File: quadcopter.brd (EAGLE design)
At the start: 136.9 x 137 mm, 62 parts, among them J1 AVR_SPI_PRG_6NS, U1 ATMEGA128RFA1, Y1 16MHz

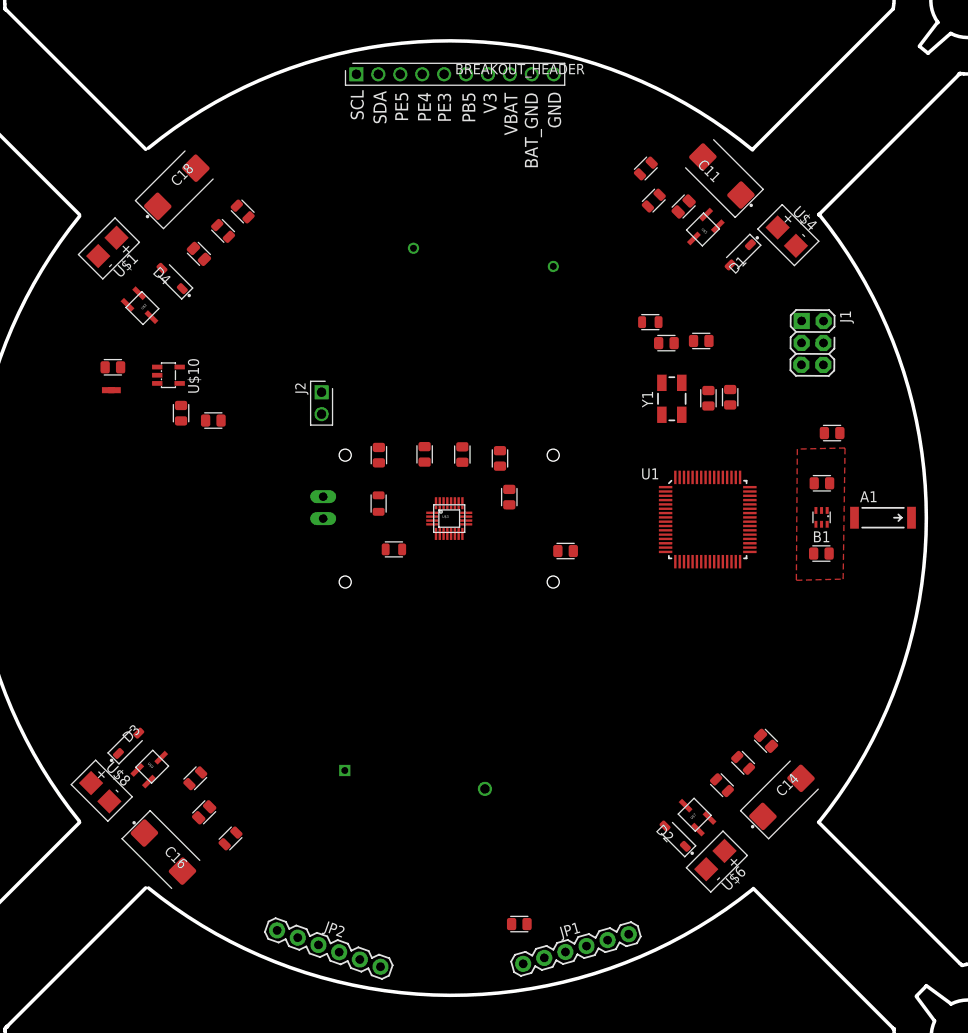
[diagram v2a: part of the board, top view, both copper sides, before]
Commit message: Trying to fix air wires
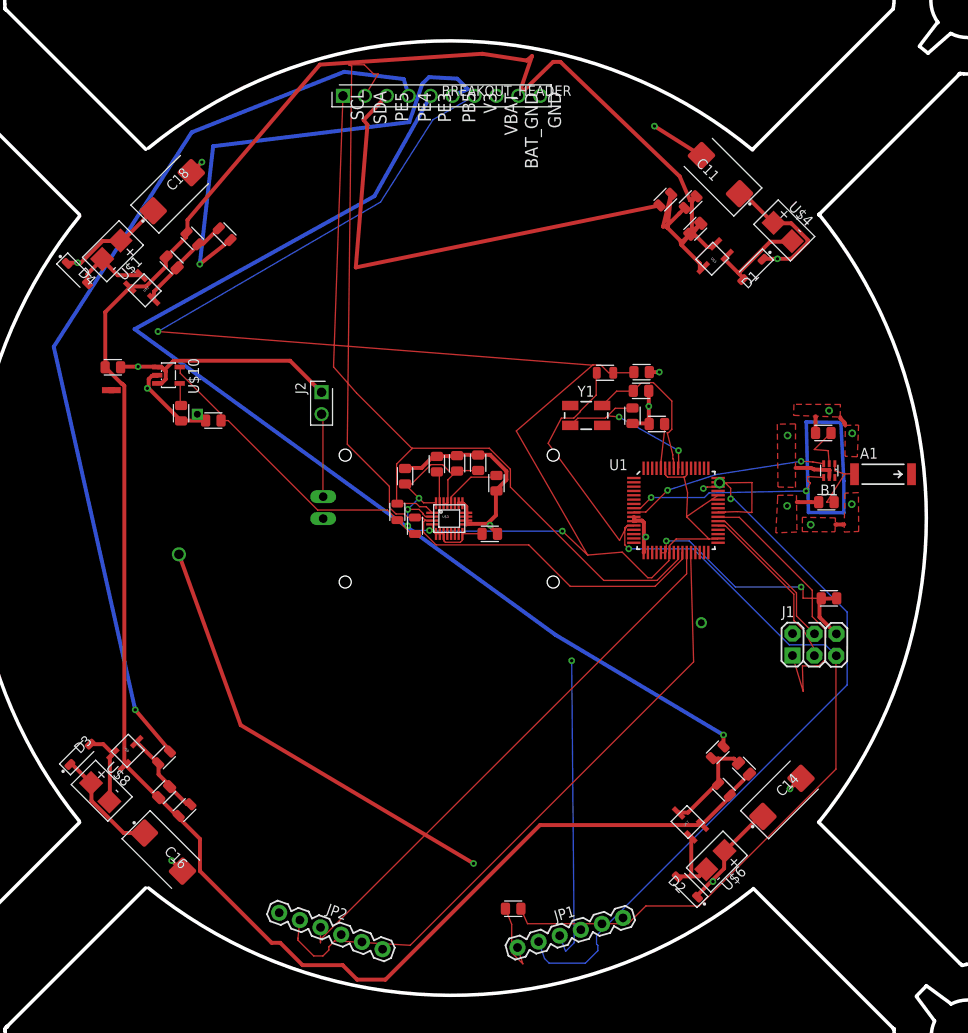
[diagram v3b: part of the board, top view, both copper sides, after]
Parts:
- moved J1 35.0 mm to (42.3, -14.6), turned to 359.7 degrees
- moved C28 19.2 mm to (44.0, -9.24)
- moved C12 14.0 mm to (43.3, 9.92)
- moved D4 11.0 mm to (-43.1, 28.4), turned to 315 degrees
- moved Y1 10.1 mm to (15.9, 11.9), turned to 0 degrees
- moved C27 9.06 mm to (22.2, 14.8)
- moved C29 9.04 mm to (24.1, 11.0), turned to 180 degrees
- moved C26 9.03 mm to (21.2, 11.9), turned to 270 degrees
- moved C5 9.00 mm to (4.70, -1.77)
- moved R1 7.88 mm to (18.1, 16.9)
- moved R6 6.49 mm to (28.0, 36.7)
- moved R10 6.26 mm to (-30.7, -33.8)
- moved D2 6.05 mm to (27.6, -42.7)
- moved D3 5.76 mm to (-42.8, -27.3)
- moved B1 5.49 mm to (44.0, 5.56)
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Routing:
- net V3: track 0.00 -> 260.9 mm, vias 0 -> 6
- net BAT_GND: track 0.00 -> 257.8 mm
- net PE3: track 0.00 -> 129.4 mm, vias 0 -> 1
- net VBAT: track 0.00 -> 123.6 mm, vias 0 -> 5
- net RESET: track 0.00 -> 118.2 mm, vias 0 -> 1
- net PE4: track 0.00 -> 107.0 mm, vias 0 -> 1
- net SDA: track 0.00 -> 102.1 mm
- net SCL: track 0.00 -> 96.4 mm
- net TX0: track 0.00 -> 82.3 mm, vias 0 -> 1
- net GND: track 0.00 -> 80.8 mm, vias 0 -> 15
- net TX1: track 0.00 -> 76.2 mm
- net RX1: track 0.00 -> 64.6 mm
- net RX0: track 0.00 -> 62.9 mm, vias 0 -> 2
- net PE5: track 0.00 -> 57.1 mm
- net PB5: track 0.00 -> 54.0 mm, vias 0 -> 1
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
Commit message: Curently updating
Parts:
- C11, C14, C16, C18: value 100uF -> 220uF
- moved C29 3.89 mm to (27.9, 10.9)
- moved R10 3.14 mm to (-27.7, -34.9)
- moved C15 3.12 mm to (-30.0, -31.0)
- moved C6 2.99 mm to (22.1, 19.9)
- moved C5 2.32 mm to (6.94, -2.37)
- moved R2 1.76 mm to (-7.77, 0.73)
- moved R1 1.72 mm to (16.4, 17.5)
- moved R12 1.52 mm to (-24.6, 32.4)
- moved R3 1.38 mm to (-4.74, -1.98)
- moved U$1 1.28 mm to (-39.3, 32.7)
- moved R9 1.06 mm to (-32.0, -27.3)
- moved C17 0.96 mm to (-5.15, 5.87)
- moved C20 0.77 mm to (-2.03, 6.79)
- moved D4 0.73 mm to (-43.7, 28.0)
- moved C21 0.66 mm to (3.38, 7.13)
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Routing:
- net PB5: track 54.0 -> 99.8 mm
- net V3: track 260.9 -> 303.3 mm
- net PE5: track 57.1 -> 83.4 mm
- net GND: track 80.8 -> 100.0 mm
- net BAT_GND: track 257.8 -> 272.0 mm
- net N$18: track 10.1 -> 20.9 mm
- net N$40: track 5.16 -> 9.04 mm
- net N$16: track 8.94 -> 12.5 mm
- net VBAT: track 123.6 -> 126.9 mm
- net SCL: track 96.4 -> 99.5 mm
- net N$1: track 11.6 -> 14.7 mm
- net SDA: track 102.1 -> 104.8 mm
- net RESET: track 118.2 -> 119.8 mm
- net N$36: track 24.5 -> 23.6 mm
- net N$21: track 3.81 -> 4.57 mm
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
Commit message: Polygon
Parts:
- moved C24 8.14 mm to (-26.7, 3.25)
- moved R4 2.50 mm to (22.6, 37.3)
- moved R7 2.22 mm to (29.1, -26.2), turned to 315 degrees
- moved C10 2.19 mm to (9.23, -44.0)
- moved U$6 1.85 mm to (32.5, -37.9)
- moved R8 1.50 mm to (30.7, -32.4)
- moved C13 1.28 mm to (35.3, -28.4)
- moved C14 1.17 mm to (39.7, -31.9)
- moved R6 1.04 mm to (27.1, 37.3)
- moved D1 1.02 mm to (34.7, 28.0)
- moved U$7 0.82 mm to (26.9, -35.6)
- moved U$5 0.70 mm to (30.7, 29.5)
- moved U$11 0.50 mm to (-38.8, 14.7)
- moved C7 0.40 mm to (28.7, 33.2)
- moved U$4 0.39 mm to (38.3, 33.2)
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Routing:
- net GND: track 100.0 -> 210.4 mm, vias 15 -> 4
- net V3: track 303.3 -> 215.4 mm, vias 6 -> 1
- net TX0: track 82.3 -> 0.00 mm, vias 1 -> 0
- net PB5: track 99.8 -> 36.1 mm
- net PE5: track 83.4 -> 34.8 mm, vias 0 -> 1
- net BAT_GND: track 272.0 -> 232.2 mm
- net PE3: track 129.1 -> 89.8 mm
- net SCL: track 99.5 -> 137.1 mm, vias 0 -> 2
- net VBAT: track 126.9 -> 100.8 mm, vias 5 -> 4
- net N$27: track 2.64 -> 21.3 mm
- net PE4: track 106.9 -> 91.0 mm
- net SDA: track 104.8 -> 91.7 mm, vias 0 -> 2
- net N$18: track 20.9 -> 14.7 mm
- net N$2: track 21.1 -> 15.1 mm
- net PB4: track 11.2 -> 5.25 mm, vias 0 -> 1
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
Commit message: Woo
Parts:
- moved C27 1.74 mm to (23.4, 16.4)
- moved C26 1.26 mm to (21.4, 13.0)
- moved C5 0.91 mm to (7.85, -2.33)
- moved C21 0.81 mm to (4.18, 7.23)
- moved C29 0.78 mm to (28.7, 11.1)
- moved C22 0.77 mm to (6.83, 4.04)
- moved R1 0.55 mm to (15.9, 17.4)
- moved C13 0.49 mm to (35.7, -28.1)
- moved R4 0.45 mm to (22.2, 37.5)
- moved R8 0.45 mm to (30.3, -32.6)
- moved C17 0.35 mm to (-4.84, 6.04)
- moved Y1 0.30 mm to (15.6, 12.0)
- moved D4 0.22 mm to (-43.6, 27.8)
- moved C6 0.19 mm to (22.0, 20.1)
- moved R3 0.14 mm to (-4.74, -2.12)
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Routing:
- net BAT_GND: track 232.2 -> 0.00 mm
- net V3: track 215.4 -> 0.00 mm, vias 1 -> 0
- net GND: track 210.4 -> 0.00 mm, vias 4 -> 0
- net SCL: track 137.1 -> 0.00 mm, vias 2 -> 0
- net RESET: track 115.3 -> 0.00 mm, vias 1 -> 0
- net VBAT: track 100.8 -> 0.00 mm, vias 4 -> 0
- net SDA: track 91.7 -> 0.00 mm, vias 2 -> 0
- net PE4: track 91.0 -> 0.00 mm, vias 1 -> 0
- net PE3: track 89.8 -> 0.00 mm, vias 1 -> 0
- net TX1: track 70.5 -> 0.00 mm, vias 1 -> 0
- net RX1: track 68.5 -> 0.00 mm, vias 1 -> 0
- net RX0: track 57.7 -> 0.00 mm, vias 1 -> 0
- net PB5: track 36.1 -> 0.00 mm, vias 1 -> 0
- net PE5: track 34.8 -> 0.00 mm, vias 1 -> 0
- net MISO: track 29.7 -> 0.00 mm
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
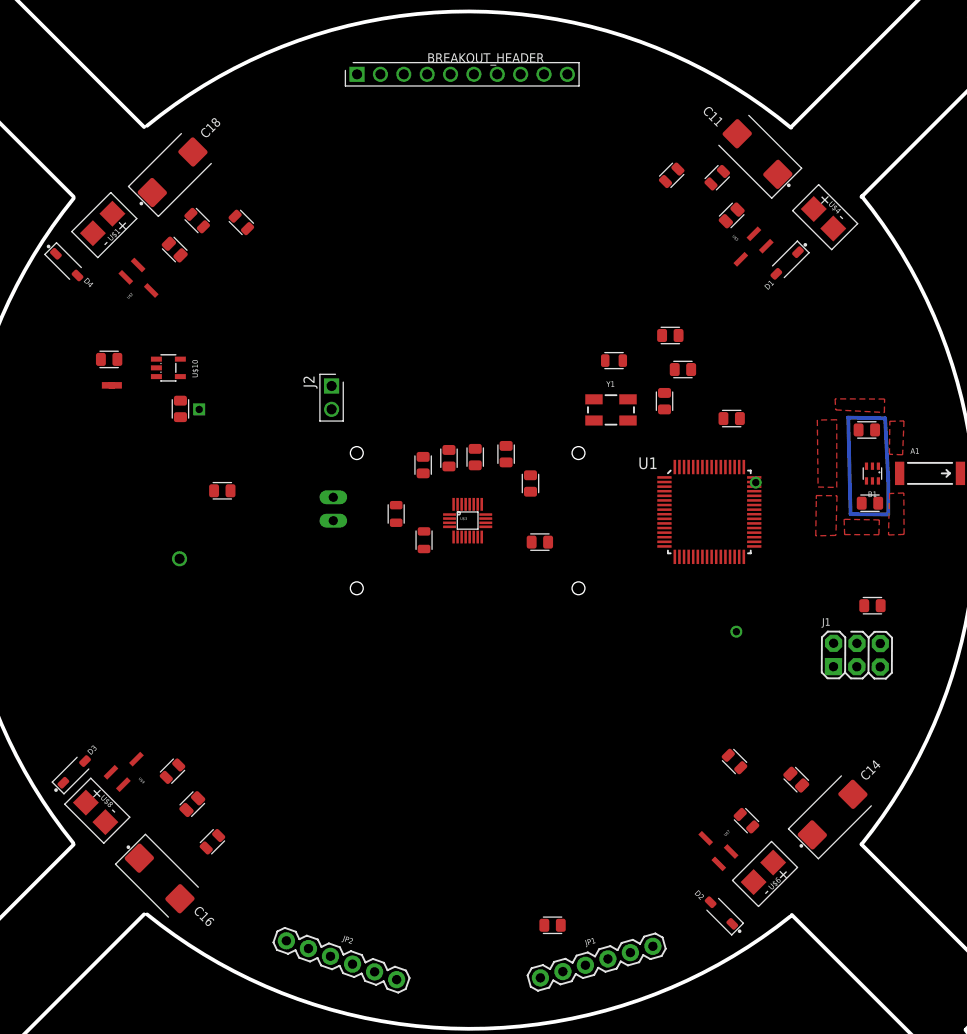
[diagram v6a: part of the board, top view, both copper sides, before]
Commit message: Yay 5 air wires and less erorrs
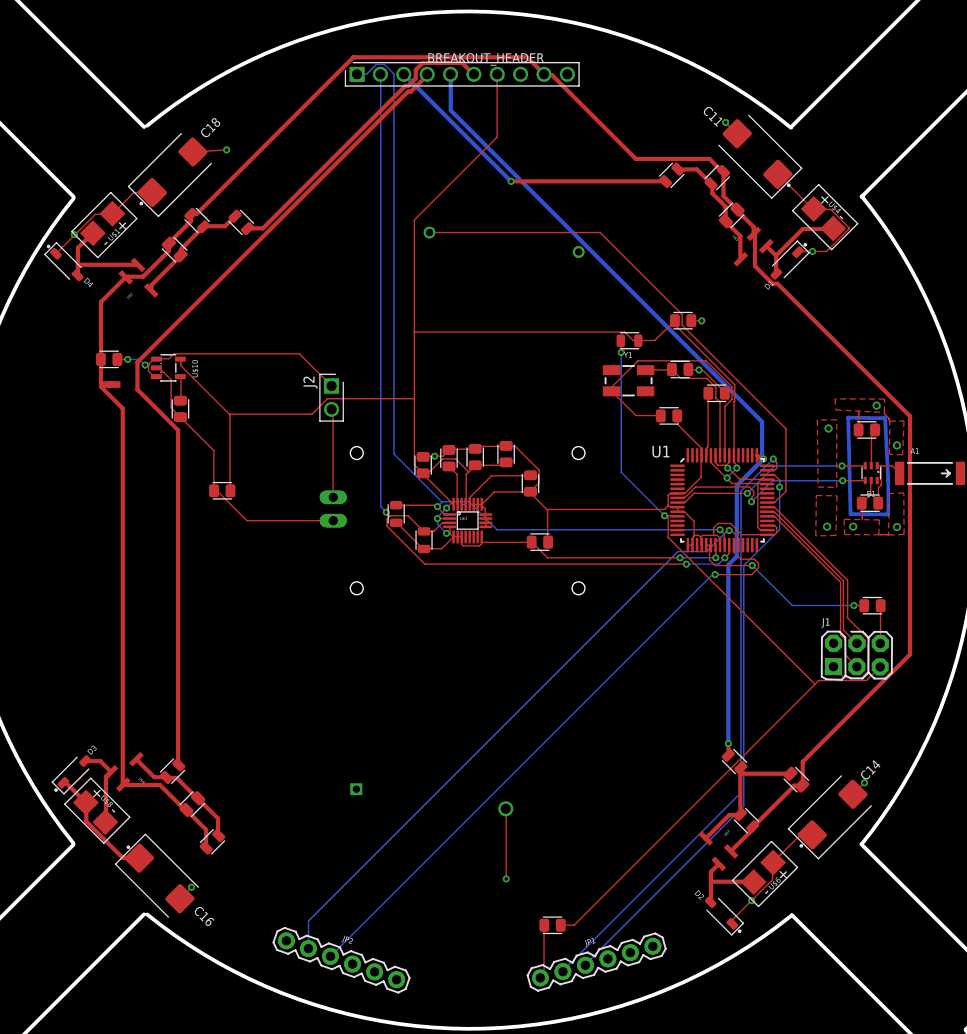
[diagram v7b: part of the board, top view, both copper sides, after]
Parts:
- moved Y1 3.70 mm to (17.5, 15.2)
- moved C29 3.20 mm to (27.1, 13.8), turned to 0 degrees
- moved R1 2.74 mm to (17.6, 19.6)
- moved C6 2.13 mm to (23.4, 21.7)
- moved U1 1.91 mm to (27.7, 2.22)
- moved C26 1.67 mm to (21.9, 11.4), turned to 0 degrees
- moved C27 0.30 mm to (23.1, 16.4)
- moved U$11 0.17 mm to (-39.0, 14.8)
- moved B1 0.14 mm to (43.9, 5.17)
- turned LR1 to 0 degrees
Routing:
- net BAT_GND: track 0.00 -> 242.4 mm
- net V3: track 0.00 -> 217.0 mm, vias 0 -> 7
- net GND: track 0.00 -> 148.8 mm, vias 0 -> 14
- net SDA: track 0.00 -> 97.6 mm, vias 0 -> 3
- net SCL: track 0.00 -> 93.9 mm, vias 0 -> 2
- net RESET: track 0.00 -> 93.7 mm, vias 0 -> 2
- net PE3: track 0.00 -> 90.6 mm, vias 0 -> 2
- net PE4: track 0.00 -> 90.2 mm
- net VBAT: track 0.00 -> 79.4 mm, vias 0 -> 6
- net TX1: track 0.00 -> 68.4 mm, vias 0 -> 1
- net RX1: track 0.00 -> 68.4 mm, vias 0 -> 1
- net TX0: track 0.00 -> 67.6 mm, vias 0 -> 1
- net RX0: track 0.00 -> 63.1 mm, vias 0 -> 1
- net PB4: track 0.00 -> 57.6 mm
- net PE5: track 0.00 -> 33.3 mm, vias 0 -> 1
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
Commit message: Almsot done with board
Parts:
- moved BREAKOUT_HEADER 8.49 mm to (-4.84, 44.0)
- moved JP1 6.63 mm to (1.30, -50.2), turned to 1.7 degrees
- moved C26 6.06 mm to (17.0, 14.9)
- moved C6 5.55 mm to (18.7, 24.6)
- moved C29 5.50 mm to (22.7, 17.2), turned to 180 degrees
- moved C27 4.94 mm to (19.5, 19.8)
- moved U1 4.62 mm to (26.0, 6.53)
- moved Y1 4.62 mm to (14.2, 18.4)
- moved U$5 3.83 mm to (34.4, 30.7)
- moved JP2 3.80 mm to (-23.1, -44.0), turned to 335 degrees
- moved R4 3.04 mm to (24.6, 35.7)
- moved C10 2.79 mm to (6.84, -42.5)
- moved R1 2.77 mm to (17.1, 22.3)
- moved R6 2.24 mm to (29.0, 36.0)
- moved C7 2.14 mm to (30.4, 31.9)
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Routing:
- net PB5: track 33.1 -> 89.3 mm, vias 0 -> 3
- net PE4: track 90.2 -> 127.8 mm, vias 0 -> 5
- net PE5: track 33.3 -> 58.9 mm, vias 1 -> 2
- net PE3: track 90.6 -> 115.0 mm
- net V3: track 217.0 -> 194.7 mm, vias 7 -> 0
- net TX0: track 67.6 -> 89.7 mm
- net BAT_GND: track 242.4 -> 261.2 mm
- net RX0: track 63.1 -> 78.3 mm
- net VBAT: track 79.4 -> 90.4 mm, vias 6 -> 5
- net N$24: track 30.1 -> 19.4 mm, vias 0 -> 4
- net TX1: track 68.4 -> 77.7 mm, vias 1 -> 2
- net PB4: track 57.6 -> 49.8 mm, vias 0 -> 2
- net MOSI: track 18.8 -> 25.3 mm
- net GND: track 148.8 -> 155.0 mm, vias 14 -> 18
- net RESET: track 93.7 -> 100.0 mm, vias 2 -> 0
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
